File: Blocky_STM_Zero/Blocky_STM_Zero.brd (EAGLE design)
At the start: 57.8 x 25.8 mm, 38 parts, among them IC3 MCP1703CB, J1 2P-2.0-90D-SMD, U1 MCP73831, U2 STM32L053R8T6, X5 8MHz(16pF)

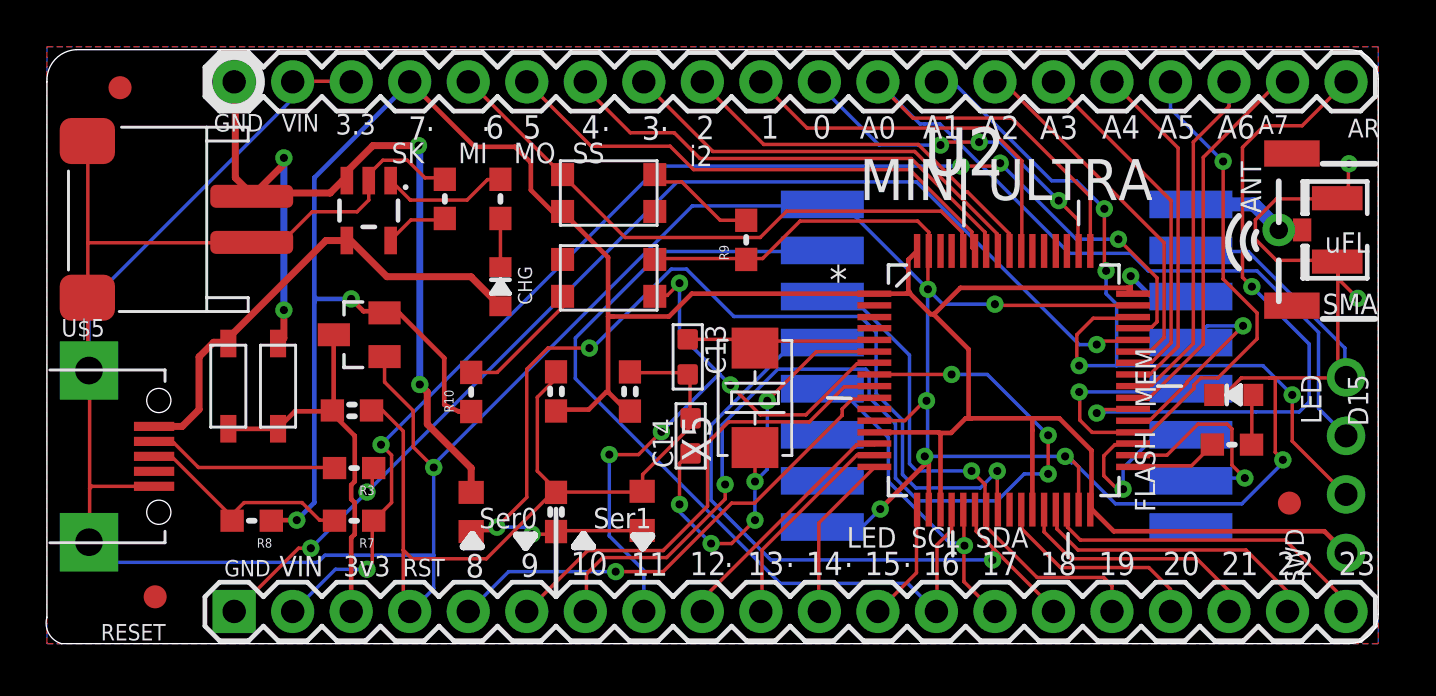
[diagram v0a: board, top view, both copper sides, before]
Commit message: Add STM Zero Board
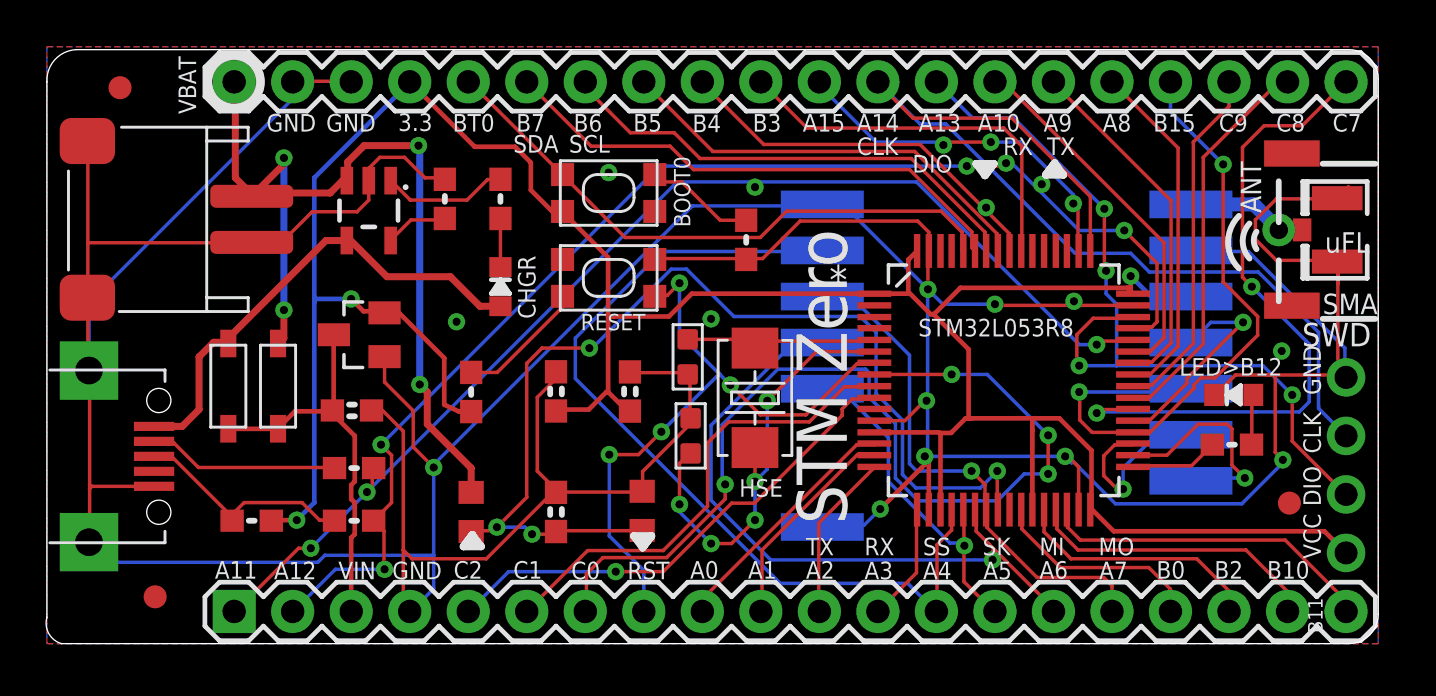
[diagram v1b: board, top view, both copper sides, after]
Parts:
- SH1, SH2: value M20 -> (none)
- X5: value 8MHz(16pF) -> 8MHz
- renumbered CHG to CHGR
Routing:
- net GND: track 249.2 -> 247.5 mm, vias 10 -> 16
- net PA12_USBDP: track 53.9 -> 55.1 mm
- net PA15: track 15.3 -> 15.8 mm
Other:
- board text added: "A10"
- board text added: "A11"
- board text added: "A12"
- board text added: "A13"
- board text added: "A14"
- board text added: "A15"
- board text added: "A8"
- board text added: "A9"
- board text added: "B0"
- board text added: "B10"
- board text added: "B11"
- board text added: "B15"
- board text added: "B2"
- board text added: "B3"
- board text added: "B4"
- board text added: "B5"
- board text added: "B6"
- board text added: "B7"
- board text added: "BOOT0"
- board text added: "BT0"
- board text added: "C0"
- board text added: "C1"
- board text added: "C2"
- board text added: "C7"
- board text added: "C8"
- board text added: "C9"
- board text added: "CLK"
- board text added: "DIO"
- board text added: "HSE"
- board text added: "LED>B12"
- board text added: "RX"
- board text added: "STM Zero"
- board text added: "STM32L053R8"
- board text added: "TX"
- board text added: "VBAT"
- board text added: "VCC"
- board text removed: "."
- board text removed: "0"
- board text removed: "1"
- board text removed: "10"
- board text removed: "11"
- board text removed: "12"
- board text removed: "13"
- board text removed: "14"
- board text removed: "15"
- board text removed: "16"
- board text removed: "17"
- board text removed: "18"
- board text removed: "19"
- board text removed: "2"
- board text removed: "20"
- board text removed: "21"
- board text removed: "22"
- board text removed: "23"
- board text removed: "3"
- board text removed: "3v3"
- board text removed: "4"
- board text removed: "5"
- board text removed: "6"
- board text removed: "7"
- board text removed: "8"
- board text removed: "9"
- board text removed: "AR"
- board text removed: "D15"
- board text removed: "D21>DIO2"
- board text removed: "D22>DIO1"
- board text removed: "D3>RST"
- board text removed: "FLASH"
- board text removed: "LED"
- board text removed: "MEM"
- board text removed: "MINI ULTRA"
- board text removed: "RX0"
- board text removed: "RX1"
- board text removed: "Ser0"
- board text removed: "Ser1"
- board text removed: "TX0"
- board text removed: "TX1"
- board text removed: "i0"
- board text removed: "i1"
- board text removed: "i2"
- board text removed: "~"
